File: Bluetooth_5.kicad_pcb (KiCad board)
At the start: 2 copper layers, 40 x 29 mm, 39 parts

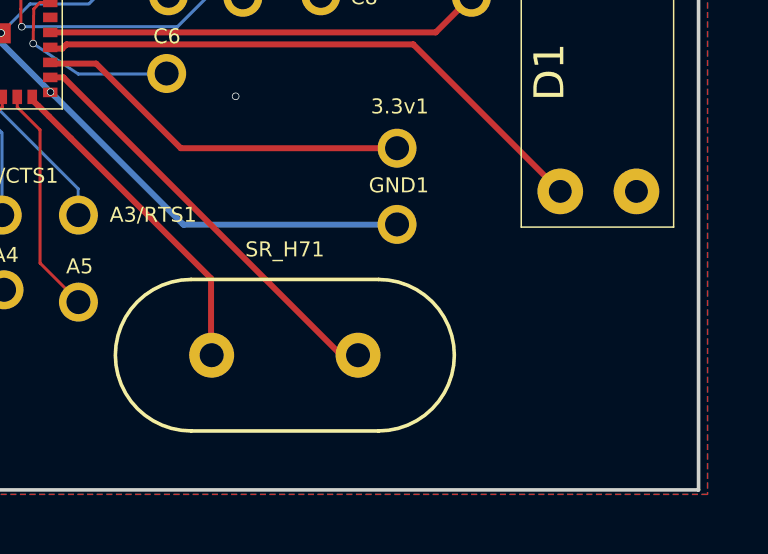
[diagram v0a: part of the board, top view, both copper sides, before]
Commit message: added datasheet and oscillator Crystal Hz
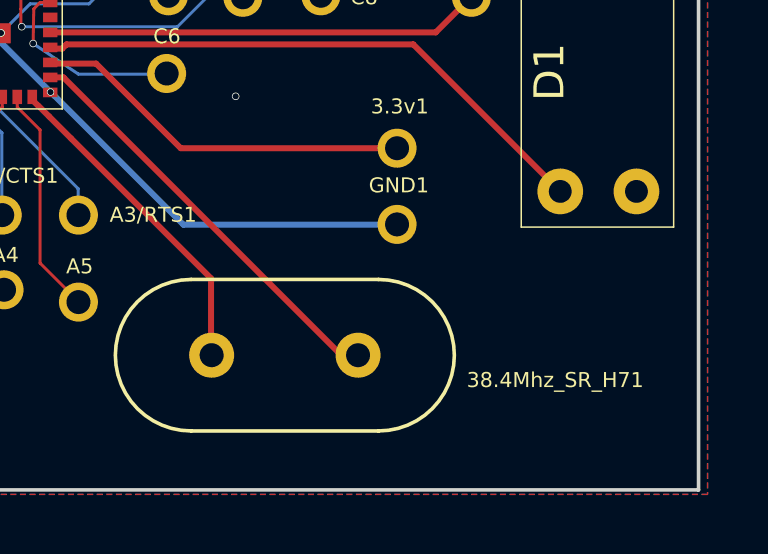
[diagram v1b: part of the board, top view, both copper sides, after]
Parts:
- renumbered SR_H71 to 38.4Mhz_SR_H71
